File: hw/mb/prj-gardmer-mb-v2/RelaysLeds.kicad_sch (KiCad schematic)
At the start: 68 parts, among them K1 AZ9371T-1A-5D, K2 AZ9371T-1A-5D, K3 AZ9371T-1A-5D, K4 AZ9371T-1A-5D, Q1 BC817, Q13 BC817, Q14 BC817, Q2 BC817, Q3 BC817, Q4 BC817, U4 74HC595, U5 74HC595, U6 ULN2803A

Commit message: Updated schematic (footprints assign), PCB and footprints: - Changed the 'Generic' footprints that were used for capacitors, resistors and fuses into specific ones (I.e. Generic_0805 is replaced by C_0805 and R_0805). - Differentiated the D_0805 and LED_0805 footprints
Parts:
- C14, C15, C16: footprint alf64:Generic_0805 -> alf64:C_0805
- D10, D11, D12, D13, D14, D5, D6, D7, D8, D9: footprint alf64:D_0805 -> alf64:LED_0805
- R16, R17, R18, R19, R20, R21, R22, R23, R24, R25, R26, R27, R28, R29, R30, R31, R48, R49, R50, R51, R52, R53: footprint alf64:Generic_0805 -> alf64:R_0805
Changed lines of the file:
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@@
 			)
 		)
-		(property "Footprint" "alf64:Generic_0805"
+		(property "Footprint" "alf64:R_0805"
 			(at 191.262 74.93 90)
 			(effects
@@
 			)
 		)
-		(property "Footprint" "alf64:Generic_0805"
+		(property "Footprint" "alf64:C_0805"
 			(at 53.0352 35.56 0)
 			(effects
@@
 			)
 		)
-		(property "Footprint" "alf64:D_0805"
+		(property "Footprint" "alf64:LED_0805"
 			(at 162.56 123.19 0)
 			(effects
@@
 			)
 		)
-		(property "Footprint" "alf64:D_0805"
+		(property "Footprint" "alf64:LED_0805"
 			(at 162.56 110.49 0)
 			(effects
@@
 			)
 		)
-		(property "Footprint" "alf64:D_0805"
+		(property "Footprint" "alf64:LED_0805"
 			(at 90.17 162.56 0)
 			(effects
@@
 			)
 		)
-		(property "Footprint" "alf64:D_0805"
+		(property "Footprint" "alf64:LED_0805"
 			(at 162.56 152.4 0)
 			(effects
@@
 			)
 		)
-		(property "Footprint" "alf64:Generic_0805"
+		(property "Footprint" "alf64:R_0805"
 			(at 184.15 137.922 90)
 			(effects
@@
 			)
 		)
-		(property "Footprint" "alf64:Generic_0805"
+		(property "Footprint" "alf64:R_0805"
 			(at 118.872 68.58 90)
 			(effects
@@
 			)
 		)
-		(property "Footprint" "alf64:Generic_0805"
+		(property "Footprint" "alf64:R_0805"
 			(at 155.702 73.66 90)
 			(effects
@@
 			)
 		)
-		(property "Footprint" "alf64:Generic_0805"
+		(property "Footprint" "alf64:R_0805"
 			(at 105.918 167.64 90)
 			(effects
@@
 			)
 		)
-		(property "Footprint" "alf64:Generic_0805"
+		(property "Footprint" "alf64:C_0805"
 			(at 65.7352 35.56 0)
 			(effects
@@
 			)
 		)
-		(property "Footprint" "alf64:Generic_0805"
+		(property "Footprint" "alf64:R_0805"
 			(at 148.59 70.358 90)
 			(effects
@@
 			)
 		)
-		(property "Footprint" "alf64:Generic_0805"
+		(property "Footprint" "alf64:R_0805"
 			(at 102.362 177.8 90)
 			(effects
@@
 			)
 		)
-		(property "Footprint" "alf64:D_0805"
+		(property "Footprint" "alf64:LED_0805"
 			(at 162.56 116.84 0)
 			(effects
@@
 			)
 		)
-		(property "Footprint" "alf64:Generic_0805"
+		(property "Footprint" "alf64:R_0805"
 			(at 184.15 115.062 90)
 			(effects
@@
 			)
 		)
-		(property "Footprint" "alf64:D_0805"
+		(property "Footprint" "alf64:LED_0805"
 			(at 162.56 139.7 0)
 			(effects
@@
 			)
 		)
-		(property "Footprint" "alf64:Generic_0805"
+		(property "Footprint" "alf64:R_0805"
 			(at 184.15 121.412 90)
 			(effects
@@
 			)
 		)
-		(property "Footprint" "alf64:Generic_0805"
+		(property "Footprint" "alf64:C_0805"
 			(at 40.3352 35.56 0)
 			(effects
@@
 			)
 		)
-		(property "Footprint" "alf64:D_0805"
+		(property "Footprint" "alf64:LED_0805"
 			(at 162.56 146.05 0)
 			(effects
@@
 			)
 		)
-		(property "Footprint" "alf64:Generic_0805"
+		(property "Footprint" "alf64:R_0805"
 			(at 111.76 65.278 90)
 			(effects
@@
 			)
 		)
-		(property "Footprint" "alf64:Generic_0805"
+		(property "Footprint" "alf64:R_0805"
 			(at 184.15 71.628 90)
 			(effects
@@
 			)
 		)
-		(property "Footprint" "alf64:D_0805"
+		(property "Footprint" "alf64:LED_0805"
 			(at 116.84 162.56 0)
 			(effects
@@
 			)
 		)
-		(property "Footprint" "alf64:Generic_0805"
+		(property "Footprint" "alf64:R_0805"
 			(at 115.062 153.67 90)
 			(effects
@@
 			)
 		)
-		(property "Footprint" "alf64:Generic_0805"
+		(property "Footprint" "alf64:R_0805"
 			(at 75.692 177.8 90)
 			(effects
@@
 			)
 		)
-		(property "Footprint" "alf64:Generic_0805"
+		(property "Footprint" "alf64:R_0805"
 			(at 79.248 167.64 90)
 			(effects
@@
 			)
 		)
-		(property "Footprint" "alf64:Generic_0805"
+		(property "Footprint" "alf64:R_0805"
 			(at 184.15 108.712 90)
 			(effects
@@
 			)
 		)
-		(property "Footprint" "alf64:Generic_0805"
+		(property "Footprint" "alf64:R_0805"
 			(at 219.71 71.628 90)
 			(effects
@@
 			)
 		)
-		(property "Footprint" "alf64:D_0805"
+		(property "Footprint" "alf64:LED_0805"
 			(at 162.56 104.14 0)
 			(effects
@@
 			)
 		)
-		(property "Footprint" "alf64:D_0805"
+		(property "Footprint" "alf64:LED_0805"
 			(at 162.56 133.35 0)
 			(effects
@@
 			)
 		)
-		(property "Footprint" "alf64:Generic_0805"
+		(property "Footprint" "alf64:R_0805"
 			(at 226.822 74.93 90)
 			(effects
@@
 			)
 		)
-		(property "Footprint" "alf64:Generic_0805"
+		(property "Footprint" "alf64:R_0805"
 			(at 88.392 153.67 90)
 			(effects
@@
 			)
 		)
-		(property "Footprint" "alf64:Generic_0805"
+		(property "Footprint" "alf64:R_0805"
 			(at 184.15 144.272 90)
 			(effects
@@
 			)
 		)
-		(property "Footprint" "alf64:Generic_0805"
+		(property "Footprint" "alf64:R_0805"
 			(at 184.15 102.362 90)
 			(effects
@@
 			)
 		)
-		(property "Footprint" "alf64:Generic_0805"
+		(property "Footprint" "alf64:R_0805"
 			(at 184.15 150.622 90)
 			(effects
@@
 			)
 		)
-		(property "Footprint" "alf64:Generic_0805"
+		(property "Footprint" "alf64:R_0805"
 			(at 184.15 131.572 90)
 			(effects

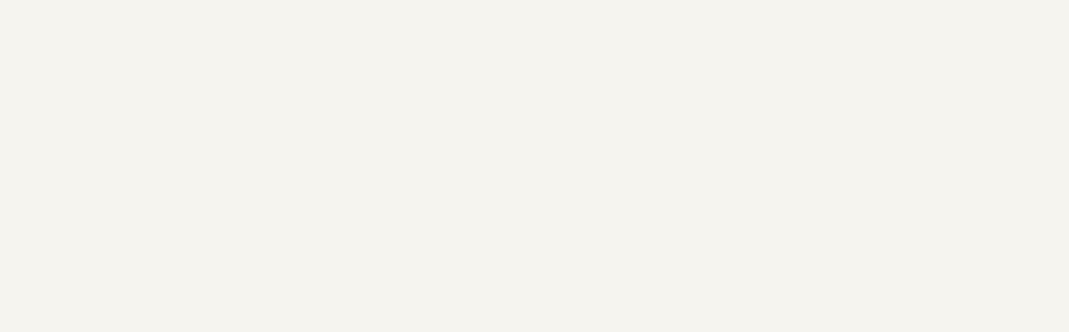
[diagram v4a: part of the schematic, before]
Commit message: Updated the hw release of prj-gardmer-mb-v2 rev001: - reorganized files in catalogues - added schematic in .pdf - added top & bottom elements on pcb in .pdf - added bom
Updated schematic:
- added a title, rev and date to the drawing info table on each sheet
- excluded test points ('TP' elements) from BOM

Updated PCB:
- added a title, rev and date to the drawing info table
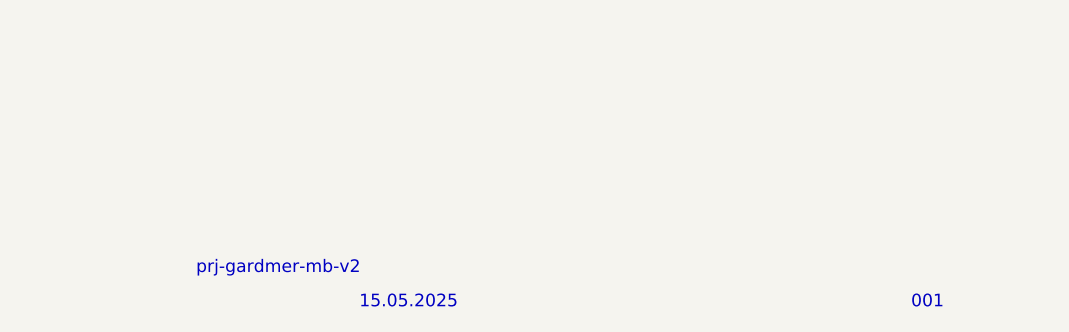
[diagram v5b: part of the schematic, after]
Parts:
- TP1, TP11, TP12, TP13, TP14, TP15, TP16, TP17, TP18, TP2, TP3, TP4, TP5, TP6, TP7, TP8: now left out of the parts list
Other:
- note added: "001"
- note added: "15.05.2025"
- note added: "prj-gardmer-mb-v2"
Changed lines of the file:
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@@
 		)
 	)
+	(text "15.05.2025"
+		(exclude_from_sim no)
+		(at 214.122 193.294 0)
+		(effects
+			(font
+				(size 1.397 1.397)
+			)
+		)
+	)
+	(text "prj-gardmer-mb-v2"
+		(exclude_from_sim no)
+		(at 199.644 189.484 0)
+		(effects
+			(font
+				(size 1.397 1.397)
+			)
+		)
+	)
+	(text "001"
+		(exclude_from_sim no)
+		(at 271.78 193.294 0)
+		(effects
+			(font
+				(size 1.397 1.397)
+			)
+		)
+	)
 	(label "SEL_LED2_EN"
 		(at 77.47 116.84 0)
@@
 		(unit 1)
 		(exclude_from_sim no)
-		(in_bom yes)
+		(in_bom no)
 		(on_board yes)
 		(dnp no)
@@
 		(unit 1)
 		(exclude_from_sim no)
-		(in_bom yes)
+		(in_bom no)
 		(on_board yes)
 		(dnp no)
@@
 		(unit 1)
 		(exclude_from_sim no)
-		(in_bom yes)
+		(in_bom no)
 		(on_board yes)
 		(dnp no)
@@
 		(unit 1)
 		(exclude_from_sim no)
-		(in_bom yes)
+		(in_bom no)
 		(on_board yes)
 		(dnp no)
@@
 		(unit 1)
 		(exclude_from_sim no)
-		(in_bom yes)
+		(in_bom no)
 		(on_board yes)
 		(dnp no)
@@
 		(unit 1)
 		(exclude_from_sim no)
-		(in_bom yes)
+		(in_bom no)
 		(on_board yes)
 		(dnp no)
@@
 		(unit 1)
 		(exclude_from_sim no)
-		(in_bom yes)
+		(in_bom no)
 		(on_board yes)
 		(dnp no)
@@
 		(unit 1)
 		(exclude_from_sim no)
-		(in_bom yes)
+		(in_bom no)
 		(on_board yes)
 		(dnp no)
@@
 		(unit 1)
 		(exclude_from_sim no)
-		(in_bom yes)
+		(in_bom no)
 		(on_board yes)
 		(dnp no)
@@
 		(unit 1)
 		(exclude_from_sim no)
-		(in_bom yes)
+		(in_bom no)
 		(on_board yes)
 		(dnp no)
@@
 		(unit 1)
 		(exclude_from_sim no)
-		(in_bom yes)
+		(in_bom no)
 		(on_board yes)
 		(dnp no)
@@
 		(unit 1)
 		(exclude_from_sim no)
-		(in_bom yes)
+		(in_bom no)
 		(on_board yes)
 		(dnp no)
@@
 		(unit 1)
 		(exclude_from_sim no)
-		(in_bom yes)
+		(in_bom no)
 		(on_board yes)
 		(dnp no)
@@
 		(unit 1)
 		(exclude_from_sim no)
-		(in_bom yes)
+		(in_bom no)
 		(on_board yes)
 		(dnp no)
@@
 		(unit 1)
 		(exclude_from_sim no)
-		(in_bom yes)
+		(in_bom no)
 		(on_board yes)
 		(dnp no)
@@
 		(unit 1)
 		(exclude_from_sim no)
-		(in_bom yes)
+		(in_bom no)
 		(on_board yes)
 		(dnp no)
